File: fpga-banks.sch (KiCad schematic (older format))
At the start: 21 parts, among them U1 XC7K70T-FBG484, U2 ASEM1-100.000MHZ-LC-T

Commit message: Add title block to the schematic sheets and some TODOs
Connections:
- wire segments 487 -> 485
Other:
- note added: "LPDDR4-TESTBED"
- note added: "SODIMM-SPECIFIC"
- note added: "TODO: Assign power rails"
- note removed: "LPDDR4"
- note removed: "SODIMM PINS"
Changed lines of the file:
@@
 encoding utf-8
 Sheet 2 8
-Title ""
+Title "LPDDR4 Test Board"
 Date ""
-Rev ""
+Rev "1.0.0"
 Comp ""
 Comment1 ""
@@
 Wire Wire Line
 	8150 9750 9025 9750
-Wire Wire Line
-	9325 9750 9675 9750
 $Comp
 L lpddr4-test-board:R_100R_0402 R6
@@
 Wire Wire Line
 	8150 10050 9025 10050
-Wire Wire Line
-	9325 10050 9675 10050
 $Comp
 L lpddr4-test-board:R_100R_0402 R7
@@
 Wire Wire Line
 	9650 9000 10200 9000
-Connection ~ 9675 9750
-Wire Wire Line
-	9675 9750 10200 9750
-Connection ~ 9675 10050
-Wire Wire Line
-	9675 10050 10200 10050
 $Comp
 L lpddr4-test-board:GND #PWR0103
@@
 	11975 2225 12100 2225
 Text Notes 11475 1000 0    98   ~ 20
-LPDDR4
+LPDDR4-TESTBED
 Wire Wire Line
 	15000 2325 15250 2325
@@
 Connection ~ 14600 1200
 Text GLabel 4600 1125 1    50   Input ~ 0
-VCC3V3
-Text GLabel 8400 1100 1    50   Input ~ 0
-VCC3V3
-Text GLabel 10075 1100 1    50   Input ~ 0
-VCC3V3
-Text GLabel 13150 1050 1    50   Input ~ 0
-VCC3V3
-Text GLabel 14750 1050 1    50   Input ~ 0
 VCC3V3
 Wire Notes Line
@@
 	6350 7950 6350 500
 Text Notes 6625 925  0    98   ~ 20
-SODIMM PINS
+SODIMM-SPECIFIC
 Text Notes 1675 850  0    98   ~ 20
 INTERFACES
@@
 Wire Wire Line
 	10250 4175 10375 4175
+Wire Wire Line
+	9325 9750 10200 9750
+Wire Wire Line
+	9325 10050 10200 10050
+Text Notes 9575 1075 2    50   ~ 0
+TODO: Assign power rails
+Text Notes 14275 1000 2    50   ~ 0
+TODO: Assign power rails
 $EndSCHEMATC

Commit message: Connect proper voltage to FPGA banks
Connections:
- net labels added: DDRVCC
- wire segments 485 -> 484
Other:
- note added: "spi-config.sch"
- note removed: "TODO: Assign power rails"
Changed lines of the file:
@@
 	4800 7100 5300 7100
 Wire Wire Line
-	10250 2275 10750 2275
-Text GLabel 10750 2275 2    50   Input ~ 0
+	1900 3600 1400 3600
+Text GLabel 1400 3600 0    50   Input ~ 0
 AD1_P
 Wire Wire Line
-	10250 2375 10750 2375
-Text GLabel 10750 2375 2    50   Input ~ 0
+	1900 3500 1400 3500
+Text GLabel 1400 3500 0    50   Input ~ 0
 AD1_N
 Wire Wire Line
-	10250 2475 10750 2475
-Text GLabel 10750 2475 2    50   Input ~ 0
+	1900 3400 1400 3400
+Text GLabel 1400 3400 0    50   Input ~ 0
 AD9_P
 Wire Wire Line
-	10250 2575 10750 2575
-Text GLabel 10750 2575 2    50   Input ~ 0
+	1900 3300 1400 3300
+Text GLabel 1400 3300 0    50   Input ~ 0
 AD9_N
 Wire Wire Line
-	10250 2675 10750 2675
-Text GLabel 10750 2675 2    50   Input ~ 0
+	1900 3200 1400 3200
+Text GLabel 1400 3200 0    50   Input ~ 0
 AD2_P
 Wire Wire Line
-	10250 2775 10750 2775
-Text GLabel 10750 2775 2    50   Input ~ 0
+	1900 3100 1400 3100
+Text GLabel 1400 3100 0    50   Input ~ 0
 AD2_N
 Wire Wire Line
-	10250 2875 10750 2875
-Text GLabel 10750 2875 2    50   Input ~ 0
+	1900 3000 1400 3000
+Text GLabel 1400 3000 0    50   Input ~ 0
 AD10_P
 Wire Wire Line
-	10250 2975 10750 2975
-Text GLabel 10750 2975 2    50   Input ~ 0
+	1900 2900 1400 2900
+Text GLabel 1400 2900 0    50   Input ~ 0
 AD10_N
 Wire Wire Line
@@
 Wire Wire Line
 	1900 3700 1850 3700
-Connection ~ 1850 3700
 Wire Wire Line
 	1850 3700 1850 3800
-Wire Wire Line
-	1900 3600 1850 3600
-Connection ~ 1850 3600
-Wire Wire Line
-	1850 3600 1850 3700
-Wire Wire Line
-	1900 3500 1850 3500
-Connection ~ 1850 3500
-Wire Wire Line
-	1850 3500 1850 3600
-Wire Wire Line
-	1900 3400 1850 3400
-Connection ~ 1850 3400
-Wire Wire Line
-	1850 3400 1850 3500
-Wire Wire Line
-	1900 3300 1850 3300
-Wire Wire Line
-	1900 3200 1850 3200
-Wire Wire Line
-	1900 3100 1850 3100
-Wire Wire Line
-	1850 3000 1900 3000
-Wire Wire Line
-	1850 2900 1900 2900
-Wire Wire Line
-	1850 2900 1850 3000
-Connection ~ 1850 3000
-Wire Wire Line
-	1850 3000 1850 3100
-Connection ~ 1850 3100
-Wire Wire Line
-	1850 3100 1850 3200
-Connection ~ 1850 3200
-Wire Wire Line
-	1850 3200 1850 3300
-Connection ~ 1850 3300
-Wire Wire Line
-	1850 3300 1850 3400
 Wire Wire Line
 	1850 4700 1850 4800
@@
 Wire Wire Line
 	1900 5900 1850 5900
-Connection ~ 1850 5900
 Wire Wire Line
 	1850 5900 1850 6000
-Wire Wire Line
-	1900 5800 1850 5800
-Connection ~ 1850 5800
-Wire Wire Line
-	1850 5800 1850 5900
-Wire Wire Line
-	1900 5700 1850 5700
-Wire Wire Line
-	1900 5600 1850 5600
-Wire Wire Line
-	1900 5500 1850 5500
-Wire Wire Line
-	1850 5400 1900 5400
 Wire Wire Line
 	1850 5300 1900 5300
@@
 Wire Wire Line
 	1850 5200 1850 5300
-Connection ~ 1850 5300
-Wire Wire Line
-	1850 5300 1850 5400
-Connection ~ 1850 5400
-Wire Wire Line
-	1850 5400 1850 5500
-Connection ~ 1850 5500
-Wire Wire Line
-	1850 5500 1850 5600
-Connection ~ 1850 5600
-Wire Wire Line
-	1850 5600 1850 5700
-Connection ~ 1850 5700
-Wire Wire Line
-	1850 5700 1850 5800
 Wire Wire Line
 	1850 6600 1850 6700
@@
 USR_LED5
 Wire Wire Line
-	1850 2900 1850 2800
-Wire Wire Line
 	1850 2800 1900 2800
-Connection ~ 1850 2900
-Text GLabel 10725 4175 2    50   Input ~ 0
-CK_RST
-Text GLabel 10725 4375 2    50   Input ~ 0
-CK_MOSI
-Text GLabel 10725 4475 2    50   Input ~ 0
-CK_MISO
-Text GLabel 10725 4575 2    50   Input ~ 0
-CK_SCK
-Text GLabel 10725 4275 2    50   Input ~ 0
-CK_SS
 Connection ~ 10300 4075
 Wire Wire Line
-	10300 4075 10300 7475
-Wire Wire Line
-	10250 4275 10725 4275
-Wire Wire Line
-	10250 4375 10725 4375
-Wire Wire Line
-	10250 4475 10725 4475
-Wire Wire Line
-	10250 4575 10725 4575
+	10300 4075 10300 4175
+Wire Wire Line
+	9325 9750 10200 9750
+Wire Wire Line
+	9325 10050 10200 10050
+Text GLabel 14750 1050 1    50   Input ~ 0
+DDRVCC
+Text GLabel 13150 1050 1    50   Input ~ 0
+DDRVCC
+Text GLabel 8400 1100 1    50   Input ~ 0
+DDRVCC
+Text GLabel 10075 1100 1    50   Input ~ 0
+DDRVCC
+Wire Wire Line
+	1900 5400 1775 5400
+Wire Wire Line
+	1425 5400 1475 5400
 $Comp
 L lpddr4-test-board:R_200R_0402 R?
 U 1 1 6B4FB04F
-P 10525 4175
-F 0 "R?" H 10350 4225 60  0000 C CNN
-F 1 "R_200R_0402" H 10525 4025 60  0001 C CNN
-F 2 "lpddr4-test-board-footprints:0402-res" H 10725 4375 60  0001 L CNN
-F 3 "" H 10525 4175 50  0001 C CNN
-F 4 "YAGEO" H 10725 4575 60  0001 L CNN "Manufacturer"
-F 5 "RC0402FR-07200RL" H 10725 4475 60  0001 L CNN "MPN"
-F 6 "200R" H 10525 4175 50  0000 C CNN "Val"
-	1    10525 4175
-	1    0    0    -1
-$EndComp
-Wire Wire Line
-	10725 4175 10675 4175
-Wire Wire Line
-	10250 4175 10375 4175
-Wire Wire Line
-	9325 9750 10200 9750
-Wire Wire Line
-	9325 10050 10200 10050
-Text Notes 9575 1075 2    50   ~ 0
-TODO: Assign power rails
-Text Notes 14275 1000 2    50   ~ 0
-TODO: Assign power rails
+P 1625 5400
+F 0 "R?" H 1475 5450 60  0000 C CNN
+F 1 "R_200R_0402" H 1625 5250 60  0001 C CNN
+F 2 "lpddr4-test-board-footprints:0402-res" H 1825 5600 60  0001 L CNN
+F 3 "" H 1625 5400 50  0001 C CNN
+F 4 "YAGEO" H 1825 5800 60  0001 L CNN "Manufacturer"
+F 5 "RC0402FR-07200RL" H 1825 5700 60  0001 L CNN "MPN"
+F 6 "200R" H 1625 5400 50  0000 C CNN "Val"
+	1    1625 5400
+	-1   0    0    -1
+$EndComp
+Wire Wire Line
+	1900 5800 1425 5800
+Wire Wire Line
+	1900 5700 1425 5700
+Wire Wire Line
+	1900 5600 1425 5600
+Wire Wire Line
+	1900 5500 1425 5500
+Text GLabel 1425 5500 0    50   Input ~ 0
+CK_SS
+Text GLabel 1425 5800 0    50   Input ~ 0
+CK_SCK
+Text GLabel 1425 5700 0    50   Input ~ 0
+CK_MISO
+Text GLabel 1425 5600 0    50   Input ~ 0
+CK_MOSI
+Text GLabel 1425 5400 0    50   Input ~ 0
+CK_RST
+Wire Wire Line
+	1850 2800 1850 3700
+Connection ~ 1850 3700
+Wire Wire Line
+	10250 2875 10300 2875
+Connection ~ 10300 2875
+Wire Wire Line
+	10300 2875 10300 2975
+Wire Wire Line
+	10250 2775 10300 2775
+Connection ~ 10300 2775
+Wire Wire Line
+	10300 2775 10300 2875
+Wire Wire Line
+	10250 2675 10300 2675
+Connection ~ 10300 2675
+Wire Wire Line
+	10300 2675 10300 2775
+Wire Wire Line
+	10250 2575 10300 2575
+Connection ~ 10300 2575
+Wire Wire Line
+	10300 2575 10300 2675
+Wire Wire Line
+	10250 2475 10300 2475
+Wire Wire Line
+	10250 2375 10300 2375
+Wire Wire Line
+	10250 2275 10300 2275
+Wire Wire Line
+	10300 2275 10300 2375
+Connection ~ 10300 2375
+Wire Wire Line
+	10300 2375 10300 2475
+Connection ~ 10300 2475
+Wire Wire Line
+	10300 2475 10300 2575
+Wire Wire Line
+	10250 2975 10300 2975
+Wire Wire Line
+	10300 2975 10300 3075
+Connection ~ 10300 3075
+Wire Wire Line
+	10250 4575 10300 4575
+Connection ~ 10300 4575
+Wire Wire Line
+	10250 4475 10300 4475
+Connection ~ 10300 4475
+Wire Wire Line
+	10300 4475 10300 4575
+Wire Wire Line
+	10250 4375 10300 4375
+Connection ~ 10300 4375
+Wire Wire Line
+	10300 4375 10300 4475
+Wire Wire Line
+	10250 4275 10300 4275
+Connection ~ 10300 4275
+Wire Wire Line
+	10300 4275 10300 4375
+Wire Wire Line
+	10250 4175 10300 4175
+Connection ~ 10300 4175
+Wire Wire Line
+	10300 4175 10300 4275
+Wire Wire Line
+	10300 4575 10300 7475
+Text Notes 875  5825 1    50   ~ 0
+spi-config.sch
+Text Notes 950  2700 1    50   ~ 0
+interfaces.sch
 $EndSCHEMATC

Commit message: Add supply remarks
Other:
- note added: "VCCO (HP banks) max: 2.0V"
- note added: "VCCO (HR banks) max: 3.6V"
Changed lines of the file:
@@
 Text Notes 950  2700 1    50   ~ 0
 interfaces.sch
+Text Notes 3225 1125 0    50   ~ 0
+VCCO (HR banks) max: 3.6V
+Text Notes 13400 1050 0    50   ~ 0
+VCCO (HP banks) max: 2.0V
+Text Notes 8700 1125 0    50   ~ 0
+VCCO (HR banks) max: 3.6V
 $EndSCHEMATC

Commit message: Update supply related circuits
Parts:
- removed C3: C_820p_0603, lpddr4-test-board-footprints:0603-res, symbol lpddr4-test-board:C_820p_0603
- added C?: C_820p_0603, antmicro-footprints:0603-res, symbol antmicroCapacitors0603:C_820p_0603
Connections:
- net labels added: VDDQ
- net labels removed: DDRVCC
- wire segments 484 -> 486
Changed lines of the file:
@@
 	8150 10600 9025 10600
-$Comp
-L lpddr4-test-board:C_820p_0603 C3
-U 1 1 60459737
-P 9675 9900
-F 0 "C3" H 9700 10000 60  0000 L CNN
-F 1 "C_820p_0603" H 9675 9750 60  0001 C CNN
-F 2 "lpddr4-test-board-footprints:0603-res" H 9875 10100 60  0001 L CNN
-F 3 "" H 9675 9900 50  0001 C CNN
-F 4 "KEMET" H 9875 10300 60  0001 L CNN "Manufacturer"
-F 5 "C0603C821J5RACTU" H 9875 10200 60  0001 L CNN "MPN"
-F 6 "820p" H 9700 9800 50  0000 L CNN "Val"
-	1    9675 9900
-	1    0    0    -1
-$EndComp
 $Comp
 L lpddr4-test-board:C_910p_0402 C1
@@
 	10300 4075 10300 4175
 Wire Wire Line
-	9325 9750 10200 9750
-Wire Wire Line
-	9325 10050 10200 10050
+	9325 9750 9675 9750
+Wire Wire Line
+	9325 10050 9675 10050
 Text GLabel 14750 1050 1    50   Input ~ 0
-DDRVCC
+VDDQ
 Text GLabel 13150 1050 1    50   Input ~ 0
-DDRVCC
-Text GLabel 8400 1100 1    50   Input ~ 0
-DDRVCC
-Text GLabel 10075 1100 1    50   Input ~ 0
-DDRVCC
+VDDQ
 Wire Wire Line
 	1900 5400 1775 5400
@@
 Text Notes 8700 1125 0    50   ~ 0
 VCCO (HR banks) max: 3.6V
+Text GLabel 8400 1100 1    50   Input ~ 0
+VCC3V3
+Text GLabel 10075 1100 1    50   Input ~ 0
+VCC3V3
+$Comp
+L antmicroCapacitors0603:C_820p_0603 C?
+U 1 1 604141EE
+P 9675 9900
+F 0 "C?" H 9790 9945 60  0000 L CNN
+F 1 "C_820p_0603" H 9675 9750 60  0001 C CNN
+F 2 "antmicro-footprints:0603-res" H 9875 10100 60  0001 L CNN
+F 3 "" H 9675 9900 50  0001 C CNN
+F 4 "KEMET" H 9875 10300 60  0001 L CNN "Manufacturer"
+F 5 "C0603C821J5RACTU" H 9875 10200 60  0001 L CNN "MPN"
+F 6 "820p" H 9790 9847 50  0000 L CNN "Val"
+	1    9675 9900
+	1    0    0    -1
+$EndComp
+Connection ~ 9675 9750
+Wire Wire Line
+	9675 9750 10200 9750
+Connection ~ 9675 10050
+Wire Wire Line
+	9675 10050 10200 10050
 $EndSCHEMATC

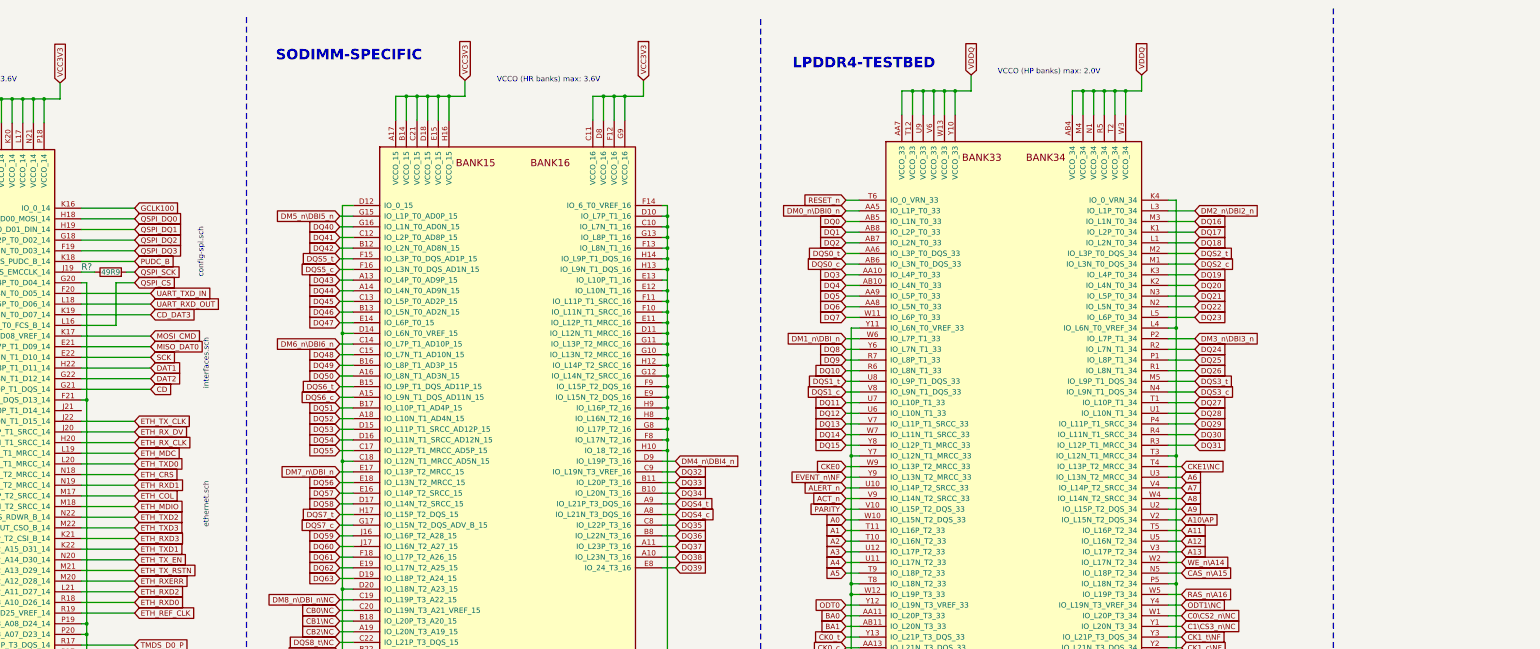
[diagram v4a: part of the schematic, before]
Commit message: Add routing between FPGA and SO-DIMM WIP
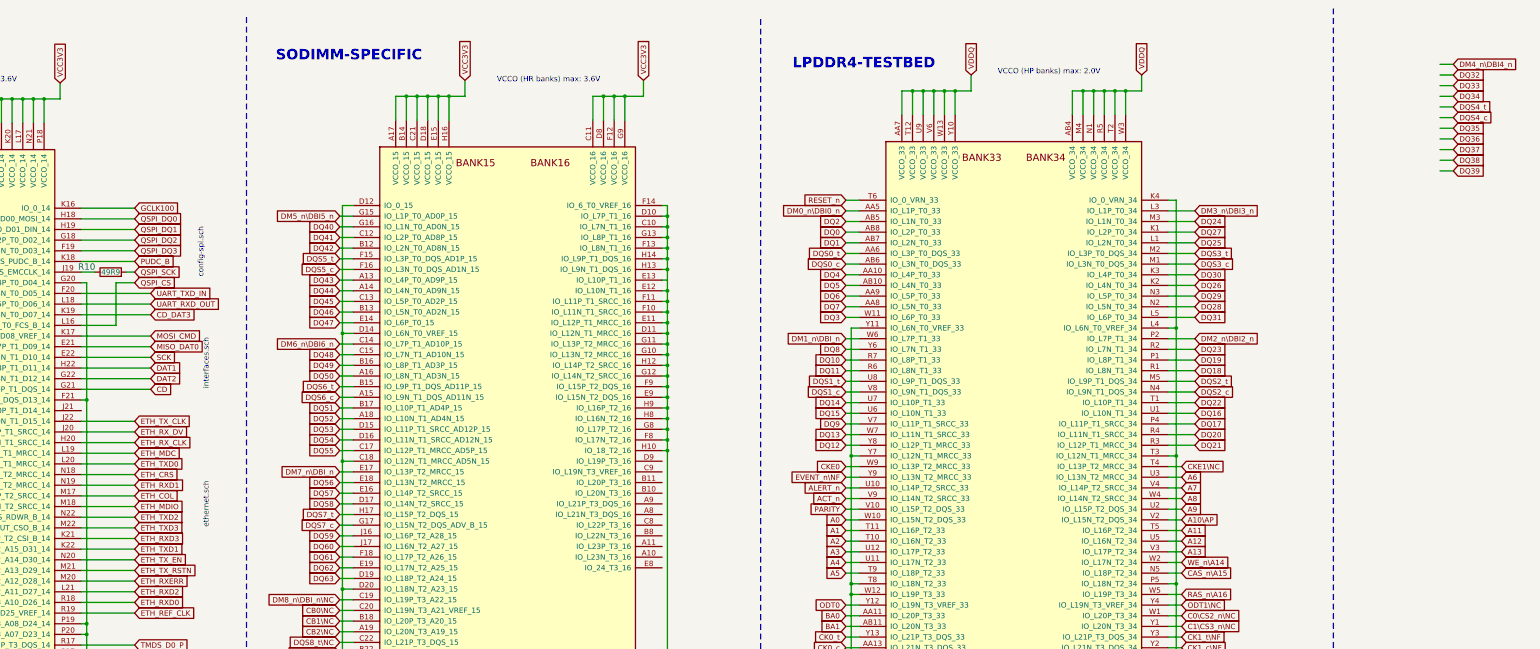
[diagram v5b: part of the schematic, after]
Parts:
- gave numbers to parts that had none: 3

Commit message: Rebuild connections to fit lpddr4 module (WIP)
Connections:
- net labels removed: CB0\NC, CB1\NC, CB2\NC, CB3\NC, CB4\NC, CB5\NC, CB6\NC, CB7\NC, DM4_n\DBI4_n, DM5_n\DBI5_n, DM6_n\DBI6_n, DM7_n\DBI_n, DM8_n\DBI_n\NC, DQ32, DQ33, DQ34, DQ35, DQ36, DQ37, DQ38, DQ39, DQ40, DQ41, DQ42, DQ43, DQ44, DQ45, DQ46, DQ47, DQ48, DQ49, DQ50, DQ51, DQ52, DQ53, DQ54, DQ55, DQ56, DQ57, DQ58, DQ59, DQ60, DQ61, DQ62, DQ63, DQS4_c, DQS4_t, DQS5_c, DQS5_t, DQS6_c, DQS6_t, DQS7_c, DQS7_t, DQS8_c\NC, DQS8_t\NC
- wire segments 486 -> 277
- no-connect marks 0 -> 133

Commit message: Add LPDDR4 routing and equalize traces - WIP
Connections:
- net labels added: CA0_A, CA0_B, CA1_A, CA1_B, CA2_A, CA2_B, CA3_A, CA3_B, CA4_A, CA4_B, CA5_A, CA5_B, CK0_N, CK0_P, CK1_N, CK1_P, CKE0_A, CKE0_B, DQS0_N, DQS0_P, DQS1_N, DQS1_P, DQS2_N, DQS2_P, DQS3_N, DQS3_P
- net labels removed: A0, A1, A10\AP, A11, A12, A13, A2, A3, A4, A5, A6, A7, A8, A9, ACT_n, ALERT_n, BA0, BA1, BG0, BG1, C0\CS2_n\NC, C1\CS3_n\NC, CAS_n\A15, CK0_c, CK0_t, CK1_c\NF, CK1_t\NF, CKE0, CKE1\NC, DQS0_c, DQS0_t, DQS1_c, DQS1_t, DQS2_c, DQS2_t, DQS3_c, DQS3_t, EVENT_n\NF, PARITY, RAS_n\A16, SA0, SA1, SA2, SCL, SDA, WE_n\A14
- wire segments 277 -> 374
- no-connect marks 133 -> 38

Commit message: Add LPDDR4 routing with equalized traces - WIP
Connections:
- net labels added: CS0_N_A, CS0_N_B, ODT1
- net labels removed: CS0_n, CS1_n\NC, ODT1\NC
- wire segments 374 -> 469
- no-connect marks 38 -> 58
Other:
- moved on the sheet: U1B
